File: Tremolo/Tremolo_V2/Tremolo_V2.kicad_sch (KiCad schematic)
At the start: 15 parts, among them J1 Barrel_Jack, J2 AudioJack2, J3 AudioJack2, U2 LM555xM

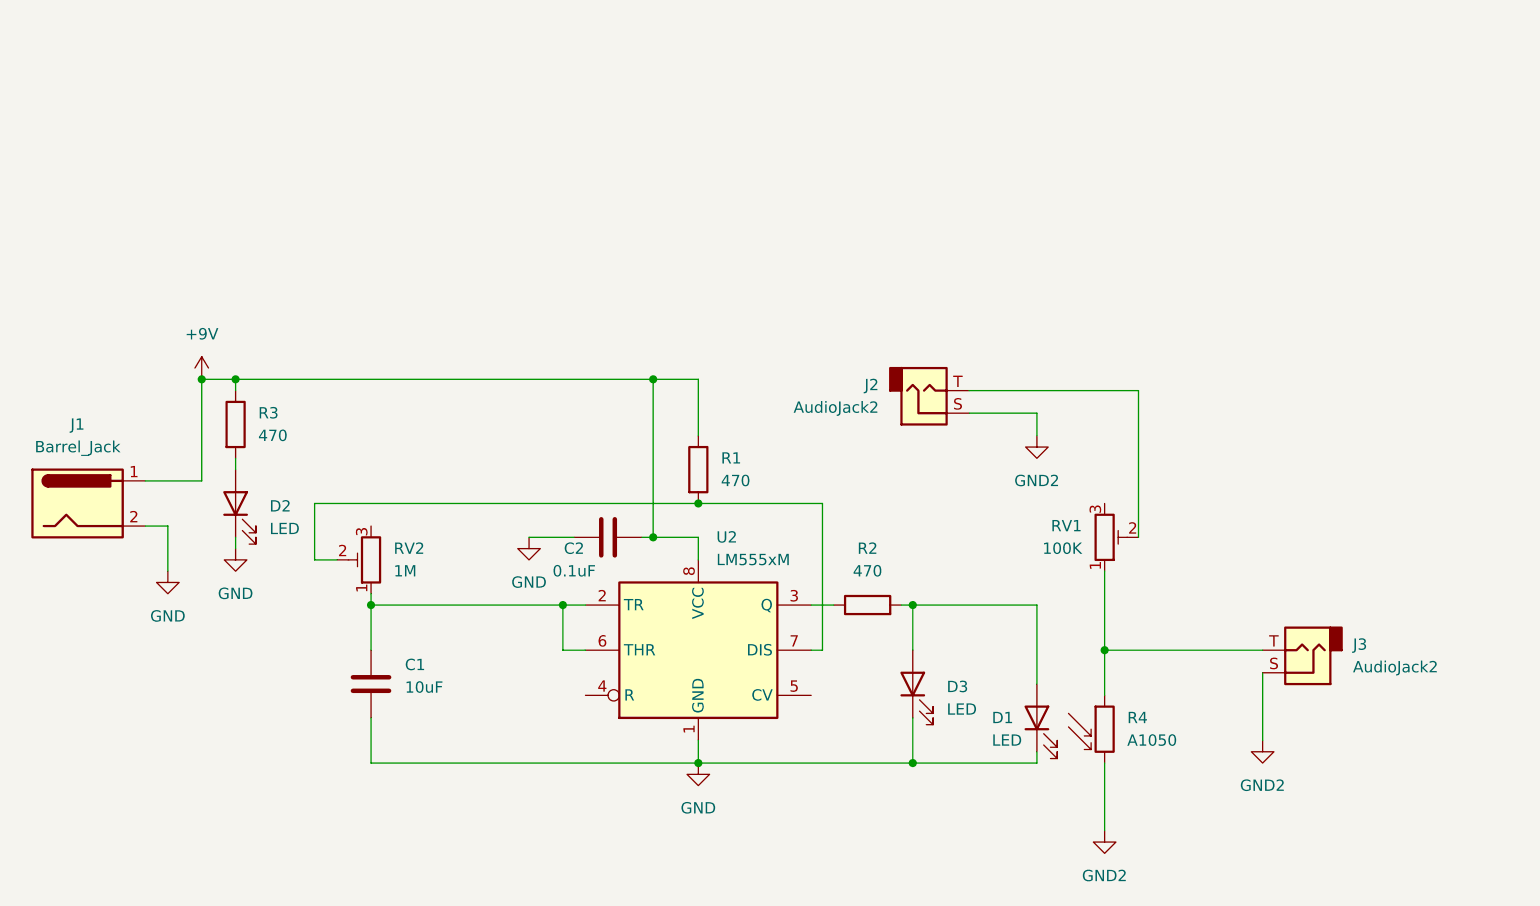
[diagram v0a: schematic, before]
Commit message: Added Tremolo enclosure CAD image
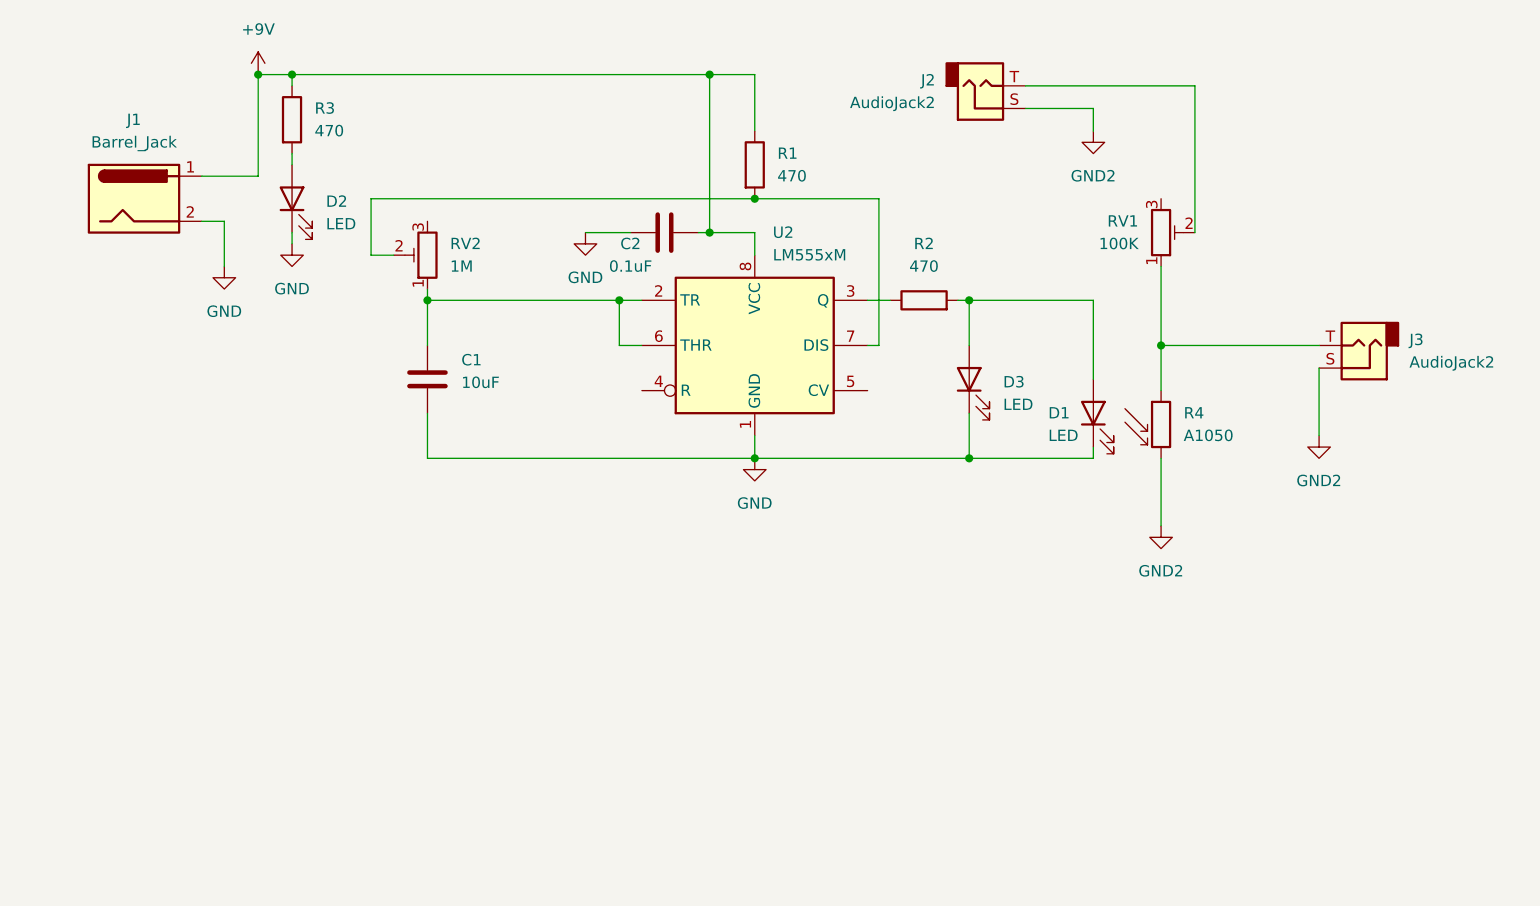
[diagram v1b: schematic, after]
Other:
- company: (none) -> EWU IEEE
- title: (none) -> Tremolo
- moved on the sheet: C1, C2, D1, D2, D3, J1, J2, J3, R1, R2, R3, R4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
